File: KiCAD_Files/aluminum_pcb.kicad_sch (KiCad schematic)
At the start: 15 parts

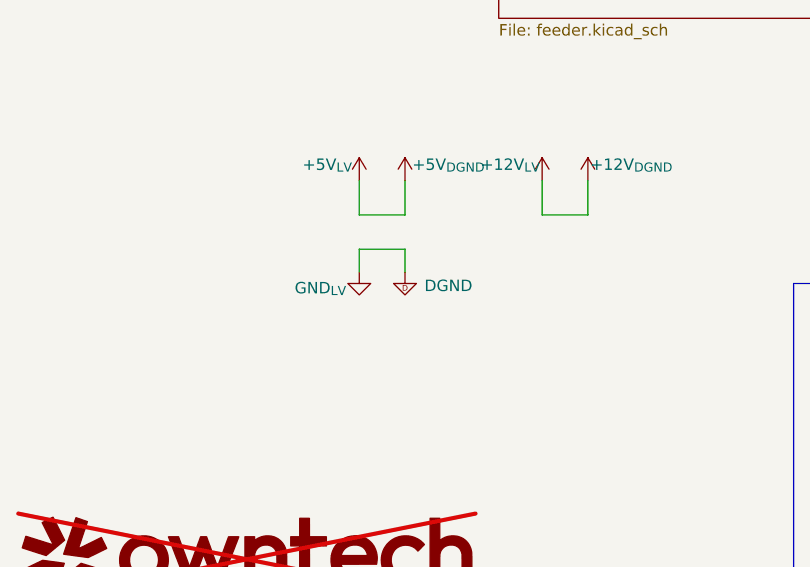
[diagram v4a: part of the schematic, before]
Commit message: Added TL431 for AC measurement 5V regulation. Added more film capacitance. Increased size of 100V ceramic caps to 1210.
Signed-off-by: Jean Alinei <jean.alinei@owntech.org>
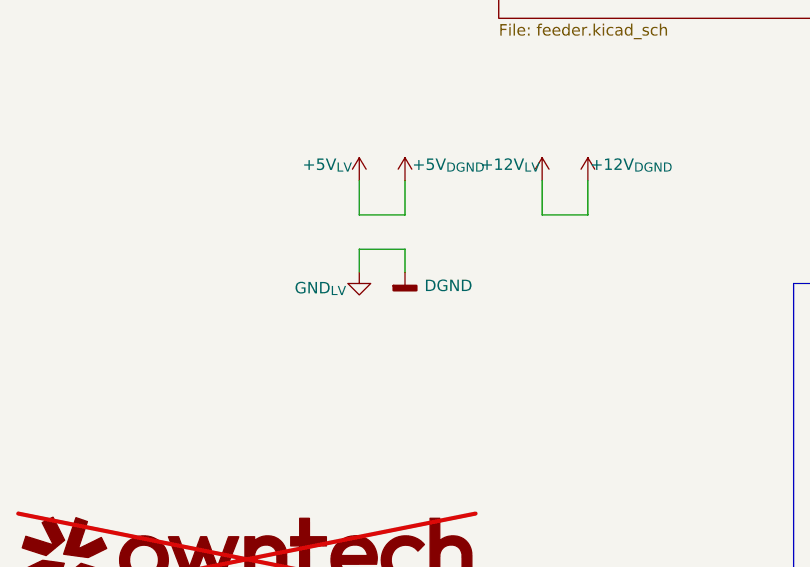
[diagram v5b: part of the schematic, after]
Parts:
- H1, H2, H3, H4, H5, H6: footprint Footprints:SMD_BD5.6-D4.1 -> Footprints:MountingHole_Pad_SMD_BD5.6-D4.1
- HS10, HS3, HS4, HS9: footprint Footprints:BTC-533-ZN01 -> Footprints:Heatsink_BTC-533-ZN01
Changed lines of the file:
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@@
 			)
 		)
-		(property "Footprint" "Footprints:BTC-533-ZN01"
+		(property "Footprint" "Footprints:Heatsink_BTC-533-ZN01"
 			(at 255.5748 181.61 0)
 			(effects
@@
 			)
 		)
-		(property "Footprint" "Footprints:SMD_BD5.6-D4.1"
+		(property "Footprint" "Footprints:MountingHole_Pad_SMD_BD5.6-D4.1"
 			(at 172.72 238.76 0)
 			(effects
@@
 			)
 		)
-		(property "Footprint" "Footprints:SMD_BD5.6-D4.1"
+		(property "Footprint" "Footprints:MountingHole_Pad_SMD_BD5.6-D4.1"
 			(at 172.72 219.71 0)
 			(effects
@@
 			)
 		)
-		(property "Footprint" "Footprints:BTC-533-ZN01"
+		(property "Footprint" "Footprints:Heatsink_BTC-533-ZN01"
 			(at 265.7348 181.61 0)
 			(effects
@@
 			)
 		)
-		(property "Footprint" "Footprints:SMD_BD5.6-D4.1"
+		(property "Footprint" "Footprints:MountingHole_Pad_SMD_BD5.6-D4.1"
 			(at 198.12 238.76 0)
 			(effects
@@
 	)
 	(symbol
-		(lib_id "Symbols:+12V_PGND")
+		(lib_id "power:+12V")
 		(at 58.42 234.95 0)
 		(unit 1)
 		(exclude_from_sim no)
-		(in_bom no)
-		(on_board no)
+		(in_bom yes)
+		(on_board yes)
 		(dnp no)
 		(property "Reference" "#PWR0129"
@@
 		)
 		(property "Footprint" ""
-			(at 61.595 232.41 0)
+			(at 58.42 234.95 0)
 			(effects
 				(font
@@
 		)
 		(property "Datasheet" ""
-			(at 61.595 232.41 0)
-			(effects
-				(font
-					(size 1.27 1.27)
-				)
-				(hide yes)
-			)
-		)
-		(property "Description" ""
+			(at 58.42 234.95 0)
+			(effects
+				(font
+					(size 1.27 1.27)
+				)
+				(hide yes)
+			)
+		)
+		(property "Description" "Power symbol creates a global label with name \"+12V\""
 			(at 58.42 234.95 0)
 			(effects
@@
 			)
 		)
-		(property "Footprint" "Footprints:SMD_BD5.6-D4.1"
+		(property "Footprint" "Footprints:MountingHole_Pad_SMD_BD5.6-D4.1"
 			(at 172.72 259.08 0)
 			(effects
@@
 			)
 		)
-		(property "Footprint" "Footprints:SMD_BD5.6-D4.1"
+		(property "Footprint" "Footprints:MountingHole_Pad_SMD_BD5.6-D4.1"
 			(at 198.12 219.71 0)
 			(effects
@@
 	)
 	(symbol
-		(lib_id "Symbols:+12V_PGND")
+		(lib_id "power:+12V")
 		(at 73.66 234.95 0)
 		(unit 1)
 		(exclude_from_sim no)
-		(in_bom no)
-		(on_board no)
+		(in_bom yes)
+		(on_board yes)
 		(dnp no)
 		(property "Reference" "#PWR0134"
@@
 		)
 		(property "Footprint" ""
-			(at 76.835 232.41 0)
+			(at 73.66 234.95 0)
 			(effects
 				(font
@@
 		)
 		(property "Datasheet" ""
-			(at 76.835 232.41 0)
-			(effects
-				(font
-					(size 1.27 1.27)
-				)
-				(hide yes)
-			)
-		)
-		(property "Description" ""
+			(at 73.66 234.95 0)
+			(effects
+				(font
+					(size 1.27 1.27)
+				)
+				(hide yes)
+			)
+		)
+		(property "Description" "Power symbol creates a global label with name \"+12V\""
 			(at 73.66 234.95 0)
 			(effects
@@
 			)
 		)
-		(property "Footprint" "Footprints:BTC-533-ZN01"
+		(property "Footprint" "Footprints:Heatsink_BTC-533-ZN01"
 			(at 235.2548 181.61 0)
 			(effects
@@
 	)
 	(symbol
-		(lib_name "GND_1")
 		(lib_id "power:GND")
 		(at 53.34 245.11 0)
@@
 	)
 	(symbol
-		(lib_id "Symbols:DGND")
+		(lib_id "power:GNDD")
 		(at 58.42 245.11 0)
 		(unit 1)
@@
 			)
 		)
-		(property "Description" ""
+		(property "Description" "Power symbol creates a global label with name \"GNDD\" , digital ground"
 			(at 58.42 245.11 0)
 			(effects
@@
 			)
 		)
-		(property "Footprint" "Footprints:BTC-533-ZN01"
+		(property "Footprint" "Footprints:Heatsink_BTC-533-ZN01"
 			(at 235.2548 198.12 0)
 			(effects
@@
 	)
 	(symbol
-		(lib_id "Symbols:+12V_PGND")
+		(lib_id "power:+12V")
 		(at 78.74 234.95 0)
 		(unit 1)
 		(exclude_from_sim no)
-		(in_bom no)
-		(on_board no)
+		(in_bom yes)
+		(on_board yes)
 		(dnp no)
 		(property "Reference" "#PWR0135"
@@
 		)
 		(property "Footprint" ""
-			(at 81.915 232.41 0)
+			(at 78.74 234.95 0)
 			(effects
 				(font
@@
 		)
 		(property "Datasheet" ""
-			(at 81.915 232.41 0)
-			(effects
-				(font
-					(size 1.27 1.27)
-				)
-				(hide yes)
-			)
-		)
-		(property "Description" ""
+			(at 78.74 234.95 0)
+			(effects
+				(font
+					(size 1.27 1.27)
+				)
+				(hide yes)
+			)
+		)
+		(property "Description" "Power symbol creates a global label with name \"+12V\""
 			(at 78.74 234.95 0)
 			(effects
@@
 	)
 	(symbol
-		(lib_id "Symbols:+12V_PGND")
+		(lib_id "power:+12V")
 		(at 53.34 234.95 0)
 		(unit 1)
 		(exclude_from_sim no)
-		(in_bom no)
-		(on_board no)
+		(in_bom yes)
+		(on_board yes)
 		(dnp no)
 		(property "Reference" "#PWR0130"
@@
 		)
 		(property "Footprint" ""
-			(at 56.515 232.41 0)
+			(at 53.34 234.95 0)
 			(effects
 				(font
@@
 		)
 		(property "Datasheet" ""
-			(at 56.515 232.41 0)
-			(effects
-				(font
-					(size 1.27 1.27)
-				)
-				(hide yes)
-			)
-		)
-		(property "Description" ""
+			(at 53.34 234.95 0)
+			(effects
+				(font
+					(size 1.27 1.27)
+				)
+				(hide yes)
+			)
+		)
+		(property "Description" "Power symbol creates a global label with name \"+12V\""
 			(at 53.34 234.95 0)
 			(effects
@@
 			)
 		)
-		(property "Footprint" "Footprints:SMD_BD5.6-D4.1"
+		(property "Footprint" "Footprints:MountingHole_Pad_SMD_BD5.6-D4.1"
 			(at 198.12 259.08 0)
 			(effects
